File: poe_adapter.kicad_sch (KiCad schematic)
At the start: 14 parts

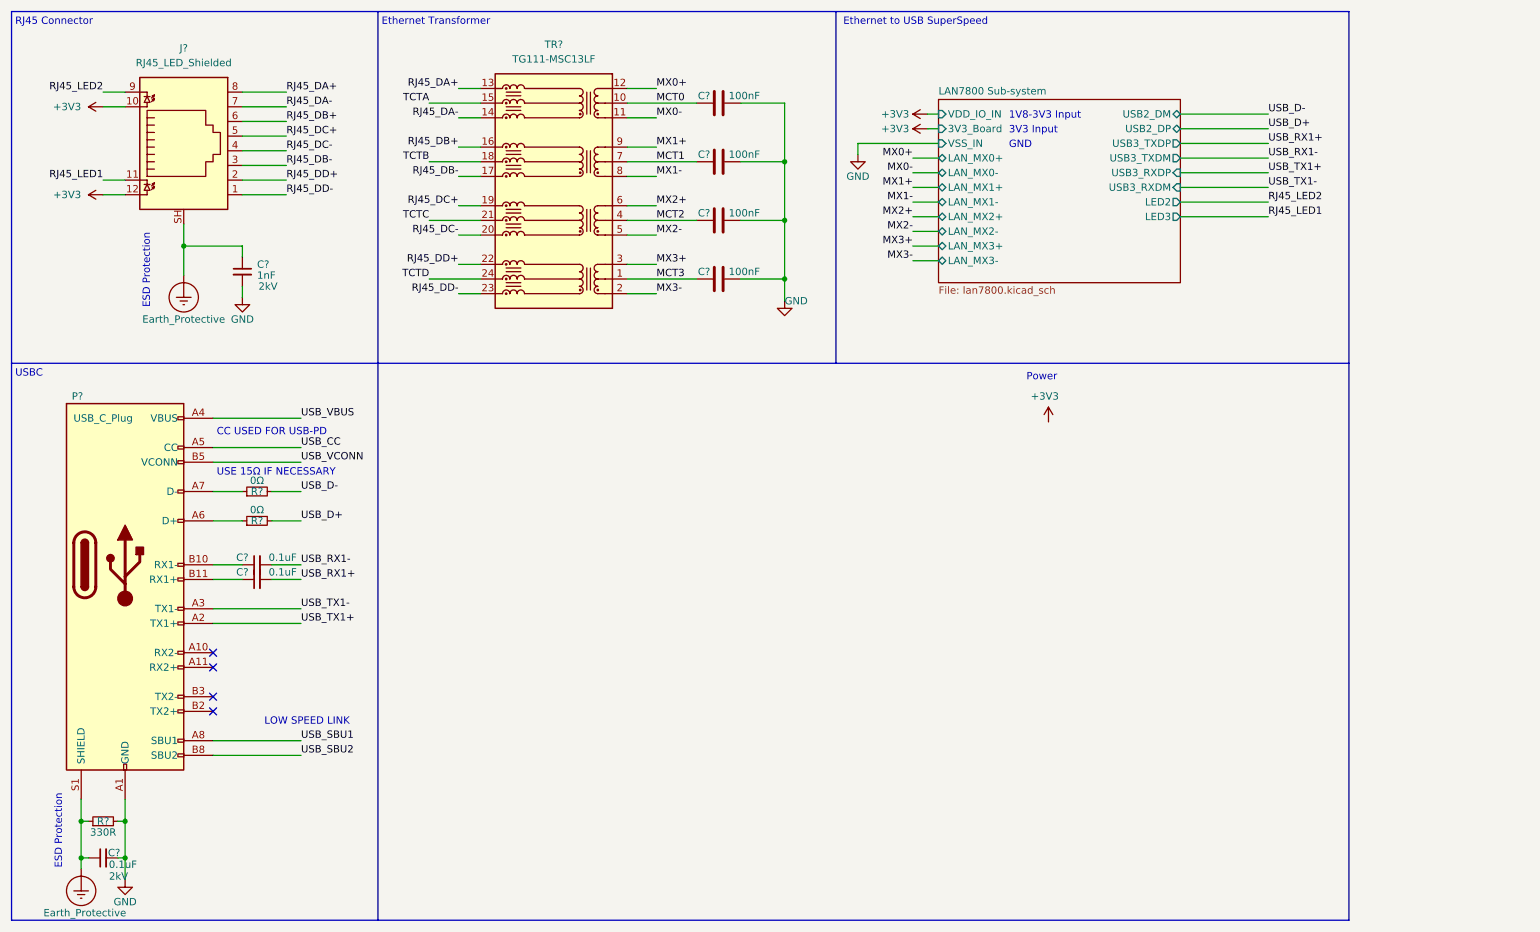
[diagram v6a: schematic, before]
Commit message: tps2372 init
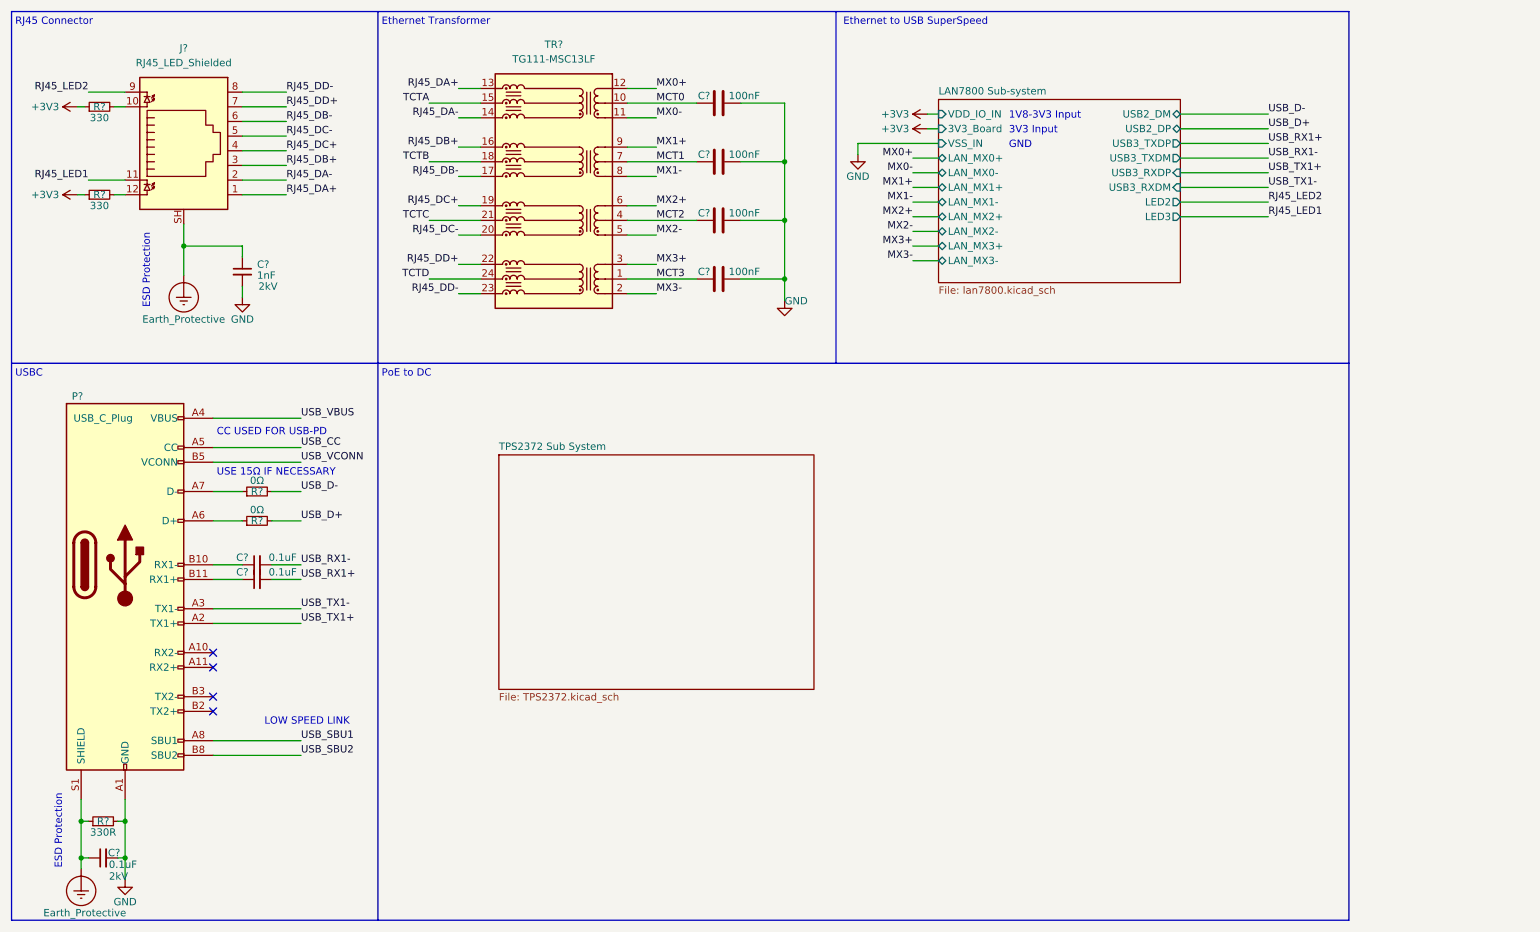
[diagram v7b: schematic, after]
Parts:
- added R? (x2): 330, symbol Device:R_Small
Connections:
- net +3V3: now also R?.1, R?.1; no longer J?.10, J?.12
- net RJ45_DA+: now also J?.1; no longer J?.8
- net RJ45_DA-: now also J?.2; no longer J?.7
- net RJ45_DB+: now also J?.3; no longer J?.6
- net RJ45_DB-: now also J?.6; no longer J?.3
- net RJ45_DC+: now also J?.4; no longer J?.5
- net RJ45_DC-: now also J?.5; no longer J?.4
- net RJ45_DD+: now also J?.7; no longer J?.2
- net RJ45_DD-: now also J?.8; no longer J?.1
- new net: J?.10, R?.2
- new net: J?.12, R?.2
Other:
- added sheet TPS2372 Sub System (TPS2372.kicad_sch)
- note added: "PoE to DC"
- note removed: "Power"

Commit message: tps2372 finish
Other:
- sheet TPS2372 Sub System ports: added PoE_48VOUT, PoE_RTN, TCTA, TCTB, TCTC, TCTD; removed none
